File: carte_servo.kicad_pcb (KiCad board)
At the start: 4 copper layers, 53.8 x 106.7 mm, 110 parts, among them J10 Conn_01x03_Male, J11 Transistor_2, J12 Transistor_1, J13 Transistor_4, J14 Transistor_.3, J16 Conn_01x04_Male, J17 Conn_01x04_Male, J18 Conn_01x03_Male, J19 Conn_01x03_Male, J2 Conn_02x04_Top_Bottom, J20 Stepper, J21 Stepper, J24 Conn_LEDs, J25 Conn_AX12, J29 Conn_AX12, J5 Conn_01x03_Male, J6 Conn_01x03_Male, J7 Conn_01x03_Male, J8 Conn_01x03_Male, J9 Conn_01x03_Male, P1 USB_C_Plug_USB2.0, Q1 DMN2011UTS, Q2 DMN2011UTS, Q3 DMN2011UTS, Q4 DMN2011UTS, Q5 DMN2011UTS, Q6 DMN2011UTS, SW1 CK_KMS2xxG, U1 XGZP6897D_differential_pressu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, U2 XGZP6897D_differential_pressu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, U3 TMC2208_SILENTSTEPSTICK, U4 TMC2208_SILENTSTEPSTICK, U5 74LVC2G241, U6 SN65HVD230, U7 LD1117S33TR_SOT223, U8 ESP32-S3-WROOM-1

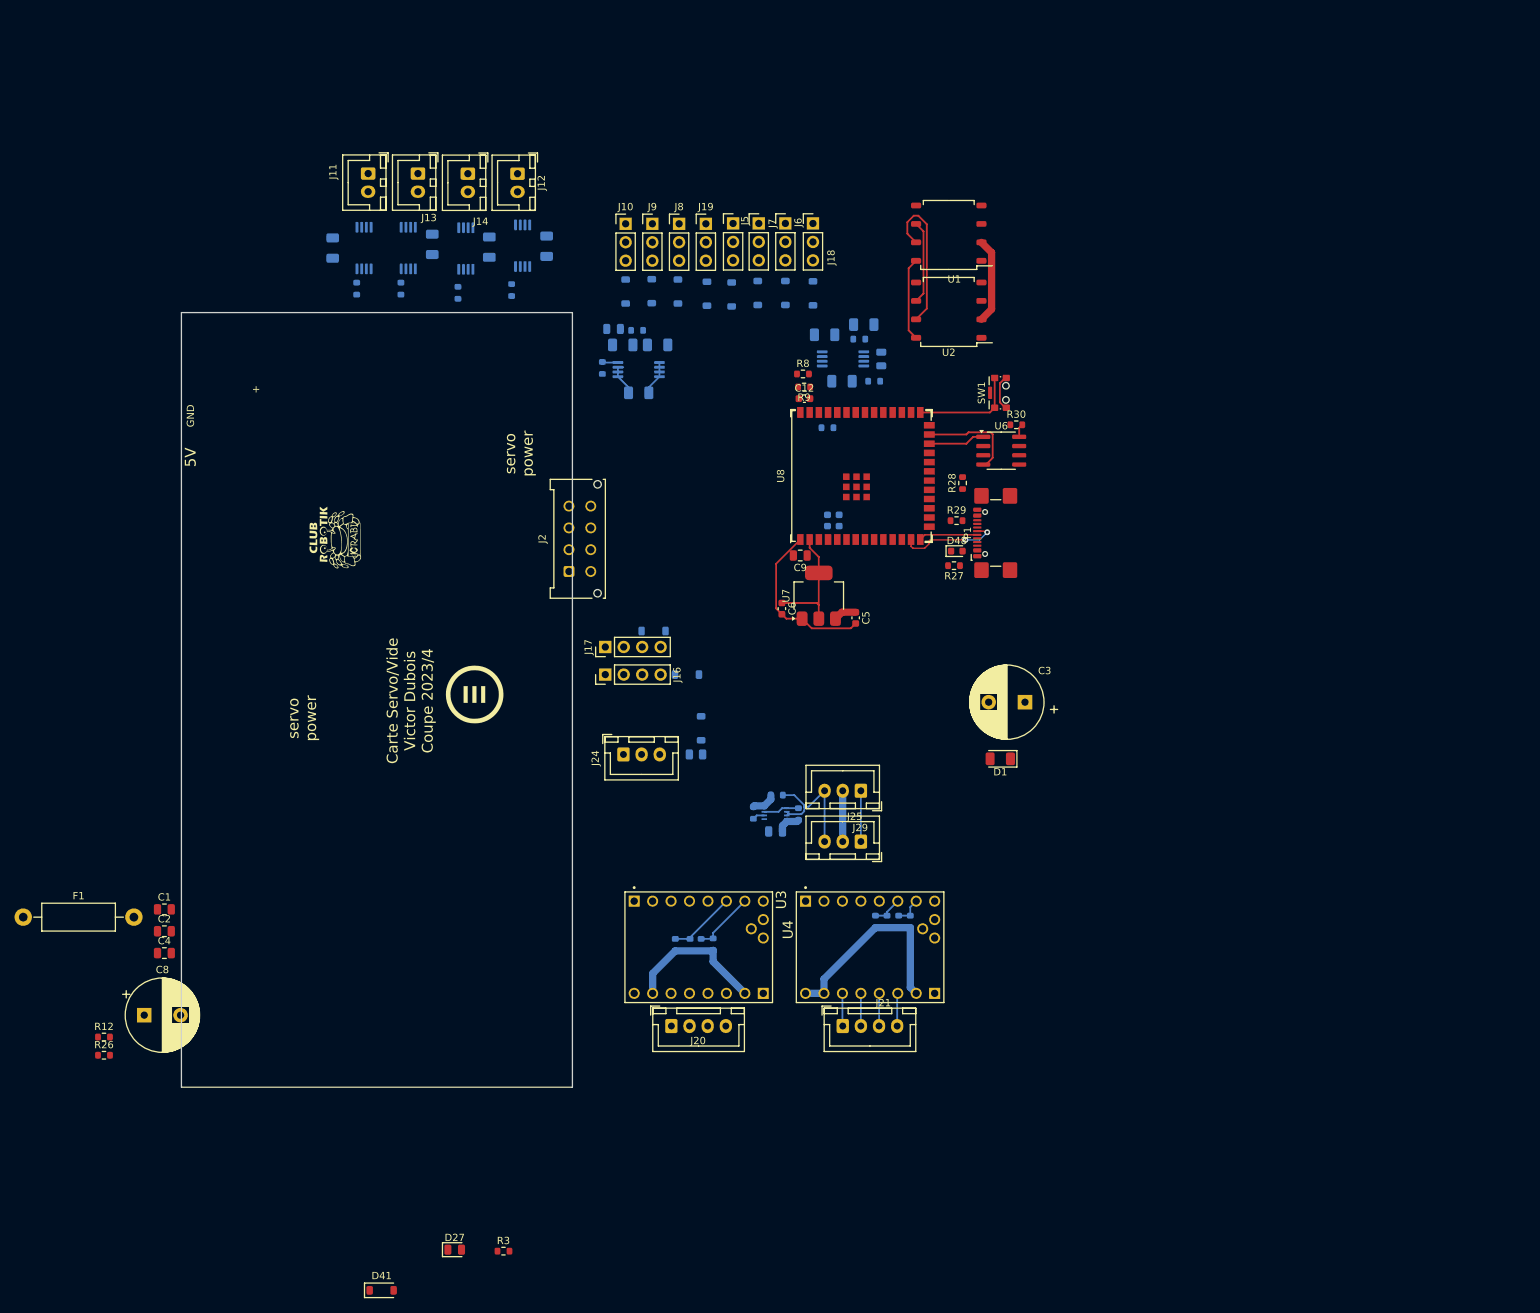
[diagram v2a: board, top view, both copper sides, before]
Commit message: add DCDC 6V
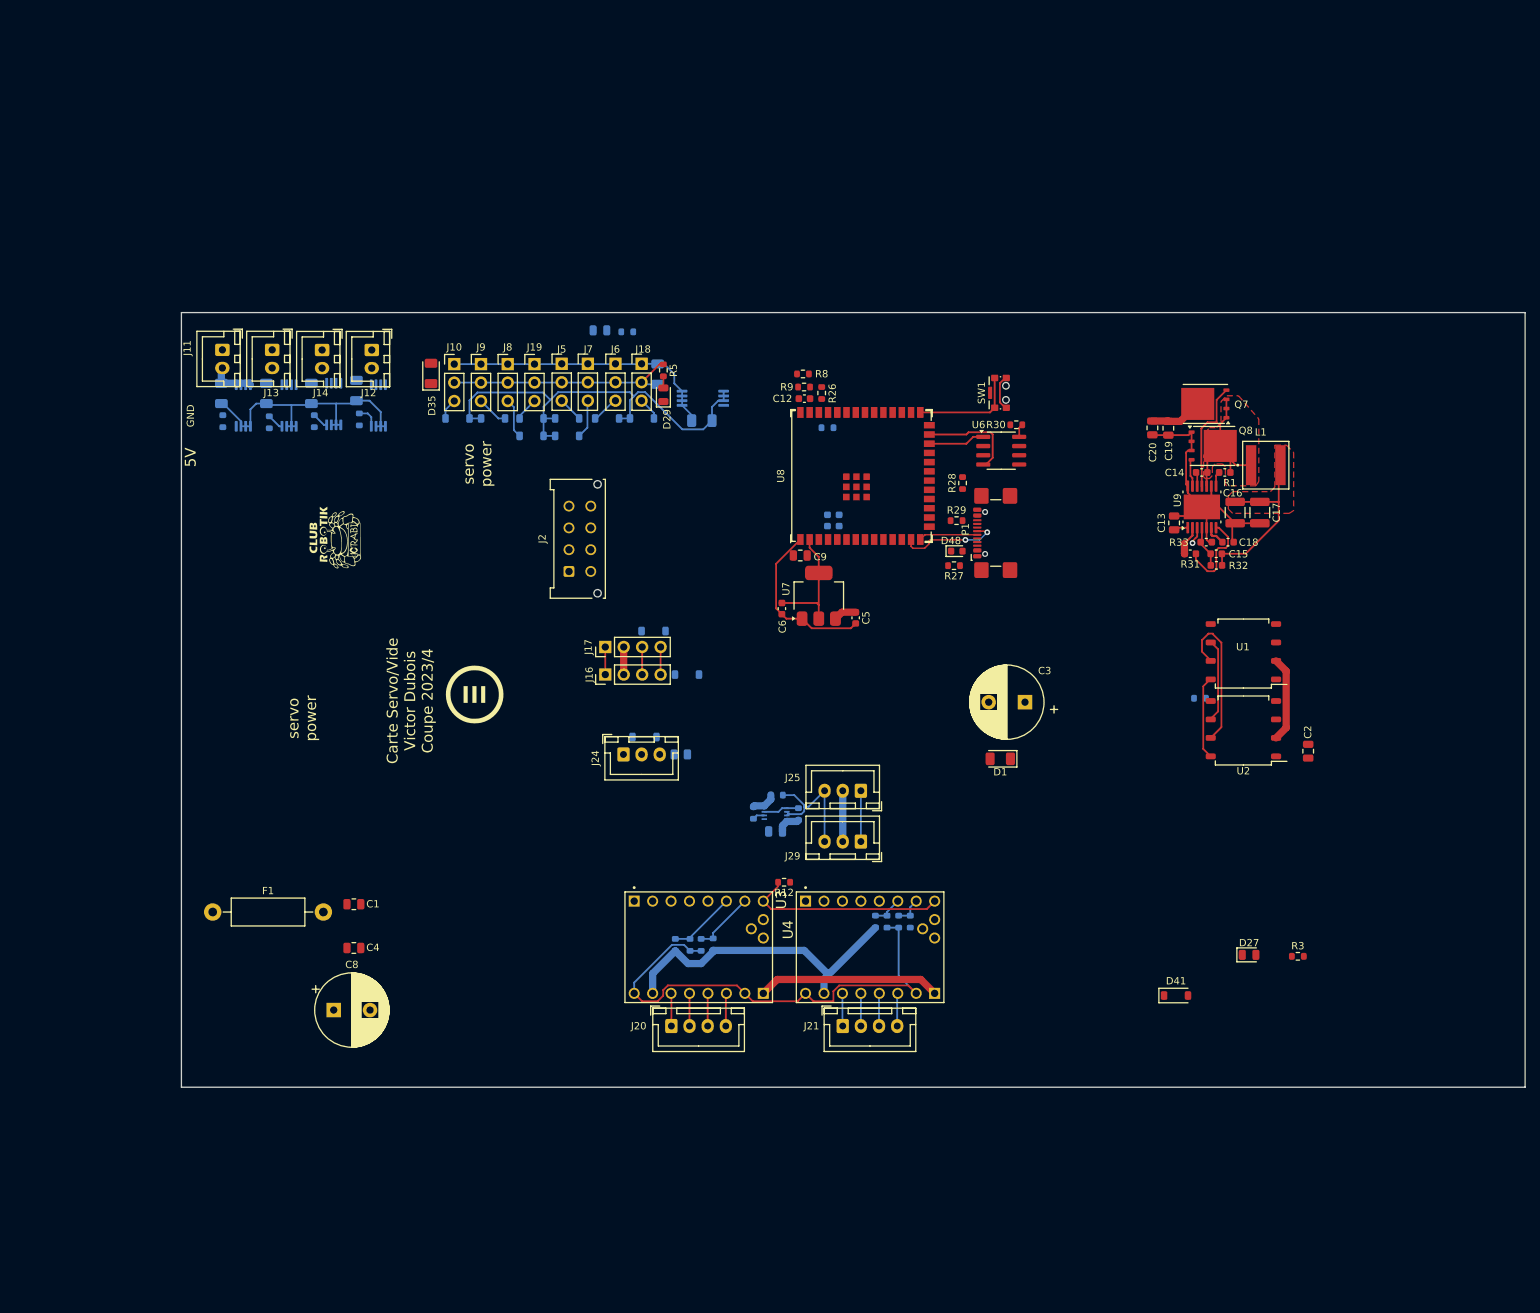
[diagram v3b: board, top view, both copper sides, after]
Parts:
- removed D2, D3: D_Zener, Diode_SMD:D_1206_3216Metric
- removed D4: D, Diode_SMD:D_1206_3216Metric
- removed Q5: DMN2011UTS, Package_SO:TSSOP-8_4.4x3mm_P0.65mm
- added C13: 2.2uF, Capacitor_SMD:C_0805_2012Metric, F.Cu at (217.7, 87.5)
- added C14: 470nF, Capacitor_SMD:C_0603_1608Metric, F.Cu at (221.5, 80.6)
- added C15: 68pF, Capacitor_SMD:C_0603_1608Metric, F.Cu at (223.5, 91.8)
- added C16: 47uF, Capacitor_SMD:C_1210_3225Metric, F.Cu at (226.1, 86.1)
- added C17: 47uF, Capacitor_SMD:C_1210_3225Metric, F.Cu at (229.5, 86.1)
- added C18: 10nF, Capacitor_SMD:C_0603_1608Metric, F.Cu at (225.2, 90.2)
- added C19: 10uF, Capacitor_SMD:C_0805_2012Metric, F.Cu at (216.9, 74.5)
- added C20: 10uF, Capacitor_SMD:C_0805_2012Metric, F.Cu at (214.7, 74.4)
- added L1: XAL6030-122MEC, XAL6030-122MEC:IND_XAL6030-122MEC, F.Cu at (230.4, 79.6)
- added Q7: CSD17307Q5A, Package_TO_SOT_SMD:TDSON-8-1, F.Cu at (222.0, 71.1)
- added Q8: CSD17579Q5A, Package_TO_SOT_SMD:TDSON-8-1, F.Cu at (223.0, 76.9)
- added R31: 52.3k, Capacitor_SMD:C_0603_1608Metric, F.Cu at (220.0, 91.8)
- added R32: 88.7k, Capacitor_SMD:C_0603_1608Metric, F.Cu at (223.6, 93.4)
- added R33: 9.76k, Capacitor_SMD:C_0603_1608Metric, F.Cu at (222.2, 90.2)
- added U9: LM3150MH, Package_SO:HTSSOP-14-1EP_4.4x5mm_P0.65mm_EP3.4x5mm_Mask3x3.1mm, F.Cu at (221.6, 85.3)
- D29, D35, R5: moved to F.Cu
- R1: value 220R -> 1.74k; footprint Resistor_SMD:R_0603_1608Metric -> Capacitor_SMD:C_0603_1608Metric; moved to F.Cu
- moved C2 159.5 mm to (236.2, 119.0), turned to 90 degrees
- moved R26 134.5 mm to (169.2, 69.6), turned to 90 degrees
- moved R3 116.7 mm to (234.8, 147.2)
- moved D27 116.7 mm to (228.1, 147.0)
- moved D41 116.7 mm to (218.0, 152.6)
- moved R12 96.1 mm to (164.0, 137.0), turned to 180 degrees
- moved R1 86.9 mm to (224.7, 80.6), turned to 0 degrees
- moved U1 70.5 mm to (227.3, 105.2)
- moved U2 70.5 mm to (227.3, 115.8)
- moved R2 62.6 mm to (221.3, 111.7)
- moved D26 32.9 mm to (105.1, 69.3)
- moved D30 32.8 mm to (134.2, 75.5), turned to 180 degrees
- moved D7 31.7 mm to (98.9, 69.7)
- moved J11 31.5 mm to (86.7, 63.7)
- moved J12 31.5 mm to (107.2, 63.7)
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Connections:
- D34 pad 1: SERVO_POWER_2 -> /ServoDCDC/VOUT
- D34 pad 2: GND_SERVO_2 -> /Servos/GND_SERVO_2
- D35 pad 1: SERVO_POWER_1 -> /ServoDCDC/VOUT
- D35 pad 2: GND_SERVO_1 -> /Servos/GND_SERVO_2
- D5 pad 1: GND_SERVO_2 -> /Servos/GND_SERVO_2
- J10 pad 1: GND_SERVO_2 -> /Servos/GND_SERVO_2
- J10 pad 2: SERVO_POWER_2 -> /ServoDCDC/VOUT
- J18 pad 1: GND_SERVO_1 -> /Servos/GND_SERVO_2
- J18 pad 2: SERVO_POWER_1 -> /ServoDCDC/VOUT
- J19 pad 1: GND_SERVO_2 -> /Servos/GND_SERVO_2
- J19 pad 2: SERVO_POWER_2 -> /ServoDCDC/VOUT
- J5 pad 1: GND_SERVO_1 -> /Servos/GND_SERVO_2
- J5 pad 2: SERVO_POWER_1 -> /ServoDCDC/VOUT
- J6 pad 1: GND_SERVO_1 -> /Servos/GND_SERVO_2
- J6 pad 2: SERVO_POWER_1 -> /ServoDCDC/VOUT
- J7 pad 1: GND_SERVO_1 -> /Servos/GND_SERVO_2
- J7 pad 2: SERVO_POWER_1 -> /ServoDCDC/VOUT
- J8 pad 1: GND_SERVO_2 -> /Servos/GND_SERVO_2
- J8 pad 2: SERVO_POWER_2 -> /ServoDCDC/VOUT
- J9 pad 1: GND_SERVO_2 -> /Servos/GND_SERVO_2
- J9 pad 2: SERVO_POWER_2 -> /ServoDCDC/VOUT
- Q6 pad 5: GND_SERVO_2 -> /Servos/GND_SERVO_2
- Q6 pad 6: GND_SERVO_2 -> /Servos/GND_SERVO_2
- Q6 pad 7: GND_SERVO_2 -> /Servos/GND_SERVO_2
- Q6 pad 8: GND_SERVO_2 -> /Servos/GND_SERVO_2
- R1 pad 1: ENABLE_SERVO_POWER_1 -> Net-(U9-ILIM)
- R1 pad 2: Net-(Q5-G) -> /ServoDCDC/SW
- R4 pad 2: SERVO_POWER_1 -> /ServoDCDC/VOUT
- R5 pad 2: SERVO_POWER_2 -> /ServoDCDC/VOUT
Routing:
- net GND: track 54.9 -> 265.2 mm
- net /ServoDCDC/VOUT: track 0.00 -> 57.6 mm
- net /Servos/GND_SERVO_2: track 0.00 -> 38.3 mm
- net BATT_12V: track 7.00 -> 43.5 mm
- net ENABLE_SERVO_POWER_1: track 0.00 -> 30.3 mm, vias 0 -> 1
- net /ServoDCDC/SW: track 0.00 -> 22.5 mm
- net Net-(Q7-G): track 0.00 -> 15.4 mm
- net Net-(U9-RON): track 0.00 -> 12.3 mm
- net TRANSISTOR_OUT_2: track 0.00 -> 6.24 mm
- net Net-(U9-FB): track 0.00 -> 5.84 mm
- net SERVO_4: track 0.00 -> 5.48 mm
- net SERVO_3: track 0.00 -> 5.32 mm
- net GND_SERVO_1: track 4.78 -> 0.00 mm
- net /stepper_driver/OA2: track 0.00 -> 4.53 mm
- net /stepper_driver/OB2: track 0.00 -> 4.52 mm
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- added copper zone on F.Cu, net /ServoDCDC/SW
- added copper zone on F.Cu, net /ServoDCDC/VOUT
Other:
- board size 53.8 x 106.7 mm -> 185 x 106.7 mm
- board text removed: "+"

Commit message: small stuff
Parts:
- C13, C14, C15, C16, C17, C18, C19, C20, L1, Q7, Q8, R1, R31, R32, R33, U9: moved to B.Cu
- moved D21 108.6 mm to (253.1, 70.2)
- moved D33 108.6 mm to (232.6, 70.2)
- moved D36 108.6 mm to (227.7, 70.2)
- moved J8 108.6 mm to (234.6, 62.7)
- moved J9 108.6 mm to (230.9, 62.7)
- moved D22 108.6 mm to (237.8, 70.2)
- moved D23 108.6 mm to (242.8, 70.2)
- moved D24 108.6 mm to (248.2, 70.2)
- moved D28 108.6 mm to (247.3, 58.1)
- moved D29 108.6 mm to (256.0, 66.9)
- moved D30 108.6 mm to (242.8, 72.6)
- moved D32 108.6 mm to (237.8, 72.6)
- moved D34 108.6 mm to (255.2, 64.1)
- moved D35 108.6 mm to (224.0, 64.0)
- moved J10 108.6 mm to (227.2, 62.7)
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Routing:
- net AX12_master_RX: track 1.69 -> 8.54 mm
- net 5V: track 65.4 -> 71.2 mm
- net /Servos/GND_SERVO_2: track 38.3 -> 34.1 mm
- net GND: track 265.2 -> 261.5 mm
- net Net-(J24-Pin_3): track 0.00 -> 3.42 mm
- net LEDs: track 0.00 -> 1.96 mm
- net /AX12_con/AX12_DATA: track 18.2 -> 19.8 mm
- added copper zone on B.Cu, net /ServoDCDC/SW
- added copper zone on B.Cu, net /ServoDCDC/VOUT
- removed copper zone on F.Cu, net /ServoDCDC/SW
- removed copper zone on F.Cu, net /ServoDCDC/VOUT
